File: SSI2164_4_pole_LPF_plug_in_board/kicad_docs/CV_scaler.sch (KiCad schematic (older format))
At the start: 7 parts, among them U4 TL072

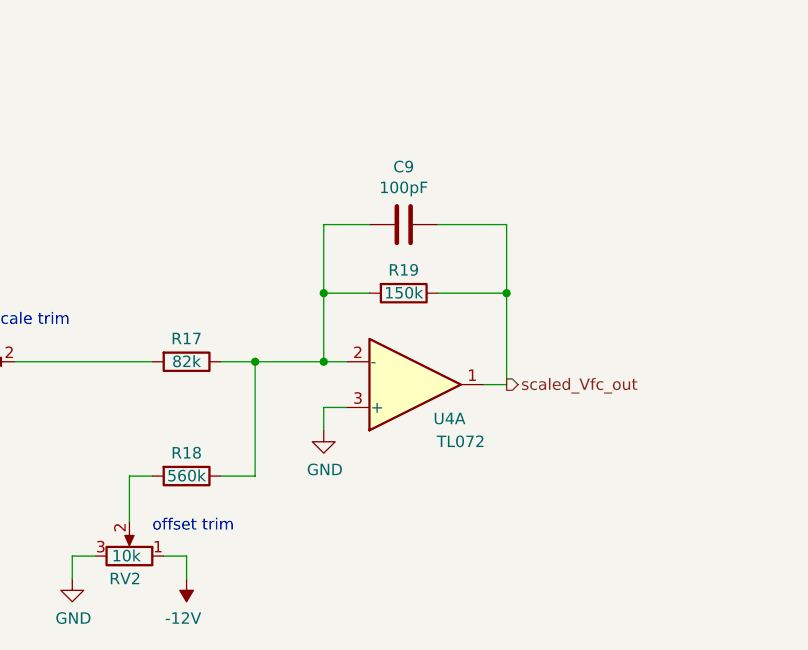
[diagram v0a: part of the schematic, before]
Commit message: progress on SSI2164 LPF
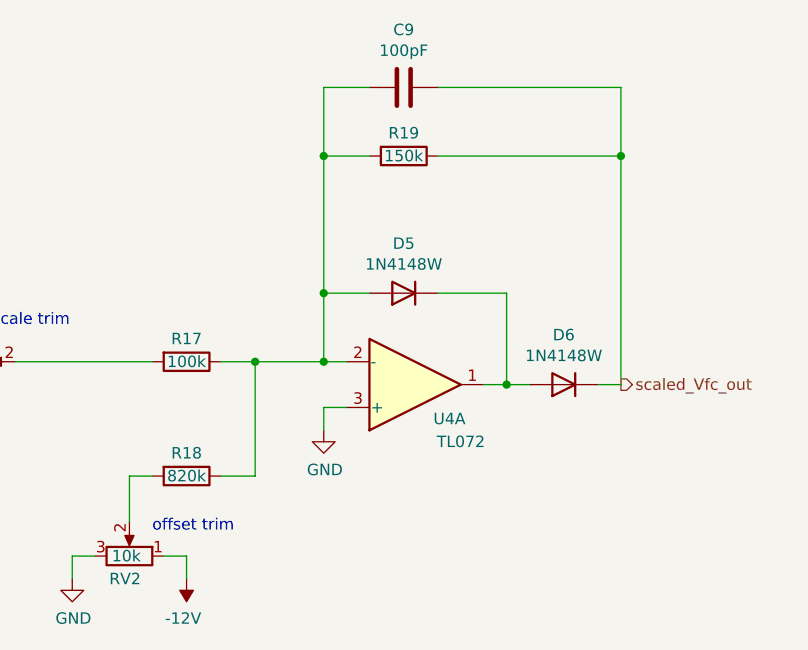
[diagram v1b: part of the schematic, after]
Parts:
- added D5, D6: 1N4148W, Diode_SMD:D_SOD-123, symbol Diode:1N4148W
- R17: value 82k -> 100k
- R18: value 560k -> 820k
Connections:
- net scaled_Vfc_out: now also D6.1 (K); no longer U4.1
- net at C9.2, R17.1, R18.1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: now also D5.2 (A)
- new net: D5.1 (K), D6.2 (A), U4.1
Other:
- moved on the sheet: C9, R19
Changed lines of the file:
@@
 L Device:R R19
 U 1 1 5F1FD667
-P 6050 2600
-F 0 "R19" V 5950 2600 50  0000 C CNN
-F 1 "150k" V 6050 2600 50  0000 C CNN
-F 2 "Resistor_SMD:R_0805_2012Metric_Pad1.15x1.40mm_HandSolder" V 5980 2600 50  0001 C CNN
-F 3 "~" H 6050 2600 50  0001 C CNN
-	1    6050 2600
+P 6050 2000
+F 0 "R19" V 5950 2000 50  0000 C CNN
+F 1 "150k" V 6050 2000 50  0000 C CNN
+F 2 "Resistor_SMD:R_0805_2012Metric_Pad1.15x1.40mm_HandSolder" V 5980 2000 50  0001 C CNN
+F 3 "~" H 6050 2000 50  0001 C CNN
+	1    6050 2000
 	0    1    1    0
 $EndComp
@@
 P 5100 2900
 F 0 "R17" V 5000 2900 50  0000 C CNN
-F 1 "82k" V 5100 2900 50  0000 C CNN
+F 1 "100k" V 5100 2900 50  0000 C CNN
 F 2 "Resistor_SMD:R_0805_2012Metric_Pad1.15x1.40mm_HandSolder" V 5030 2900 50  0001 C CNN
 F 3 "~" H 5100 2900 50  0001 C CNN
@@
 P 5100 3400
 F 0 "R18" V 5000 3400 50  0000 C CNN
-F 1 "560k" V 5100 3400 50  0000 C CNN
+F 1 "820k" V 5100 3400 50  0000 C CNN
 F 2 "Resistor_SMD:R_0805_2012Metric_Pad1.15x1.40mm_HandSolder" V 5030 3400 50  0001 C CNN
 F 3 "~" H 5100 3400 50  0001 C CNN
@@
 	5700 2900 5700 2600
 Wire Wire Line
-	5700 2600 5900 2600
-Wire Wire Line
-	6400 3000 6500 3000
-Wire Wire Line
-	6500 3000 6500 2600
-Wire Wire Line
-	6500 2600 6200 2600
+	5700 2000 5900 2000
 Wire Wire Line
 	5700 2900 5400 2900
@@
 L Device:C C9
 U 1 1 5F20EF6F
-P 6050 2300
-F 0 "C9" V 5798 2300 50  0000 C CNN
-F 1 "100pF" V 5889 2300 50  0000 C CNN
-F 2 "Capacitor_SMD:C_0805_2012Metric_Pad1.15x1.40mm_HandSolder" H 6088 2150 50  0001 C CNN
-F 3 "~" H 6050 2300 50  0001 C CNN
-	1    6050 2300
-	0    1    1    0
-$EndComp
-Wire Wire Line
-	5900 2300 5700 2300
-Wire Wire Line
-	5700 2300 5700 2600
-Connection ~ 5700 2600
-Wire Wire Line
-	6200 2300 6500 2300
-Wire Wire Line
-	6500 2300 6500 2600
-Connection ~ 6500 2600
+P 6050 1700
+F 0 "C9" V 5798 1700 50  0000 C CNN
+F 1 "100pF" V 5889 1700 50  0000 C CNN
+F 2 "Capacitor_SMD:C_0805_2012Metric_Pad1.15x1.40mm_HandSolder" H 6088 1550 50  0001 C CNN
+F 3 "~" H 6050 1700 50  0001 C CNN
+	1    6050 1700
+	0    1    1    0
+$EndComp
+Wire Wire Line
+	5900 1700 5700 1700
+Wire Wire Line
+	5700 1700 5700 2000
+Connection ~ 5700 2000
 Text HLabel 4050 2650 0    50   Input ~ 0
 raw_Vfc_in
@@
 Wire Wire Line
 	4200 2650 4200 2750
-Text HLabel 6500 3000 2    50   Output ~ 0
+Text HLabel 7000 3000 2    50   Output ~ 0
 scaled_Vfc_out
 Text Notes 4250 2750 0    50   ~ 0
@@
 Text Notes 5800 6650 0    50   ~ 0
 unused
+$Comp
+L Diode:1N4148W D5
+U 1 1 5F3AFC17
+P 6050 2600
+F 0 "D5" H 6050 2383 50  0000 C CNN
+F 1 "1N4148W" H 6050 2474 50  0000 C CNN
+F 2 "Diode_SMD:D_SOD-123" H 6050 2425 50  0001 C CNN
+F 3 "https://www.vishay.com/docs/85748/1n4148w.pdf" H 6050 2600 50  0001 C CNN
+	1    6050 2600
+	-1   0    0    1
+$EndComp
+$Comp
+L Diode:1N4148W D6
+U 1 1 5F3B1278
+P 6750 3000
+F 0 "D6" H 6750 2783 50  0000 C CNN
+F 1 "1N4148W" H 6750 2874 50  0000 C CNN
+F 2 "Diode_SMD:D_SOD-123" H 6750 2825 50  0001 C CNN
+F 3 "https://www.vishay.com/docs/85748/1n4148w.pdf" H 6750 3000 50  0001 C CNN
+	1    6750 3000
+	-1   0    0    1
+$EndComp
+Wire Wire Line
+	6600 3000 6500 3000
+Wire Wire Line
+	6500 3000 6500 2600
+Wire Wire Line
+	6500 2600 6200 2600
+Connection ~ 6500 3000
+Wire Wire Line
+	6500 3000 6400 3000
+Wire Wire Line
+	5900 2600 5700 2600
+Connection ~ 5700 2600
+Wire Wire Line
+	5700 2600 5700 2000
+Wire Wire Line
+	6900 3000 7000 3000
+Wire Wire Line
+	7000 3000 7000 2000
+Wire Wire Line
+	7000 1700 6200 1700
+Wire Wire Line
+	6200 2000 7000 2000
+Connection ~ 7000 2000
+Wire Wire Line
+	7000 2000 7000 1700
 $EndSCHEMATC
